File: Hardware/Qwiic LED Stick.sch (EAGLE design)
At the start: 39 parts, among them J2 SMD, J3 PTH, J4 SMD, J6 AVR_SPI_PROG_3X2TESTPOINTS, U1 Tiny85-20-SMT

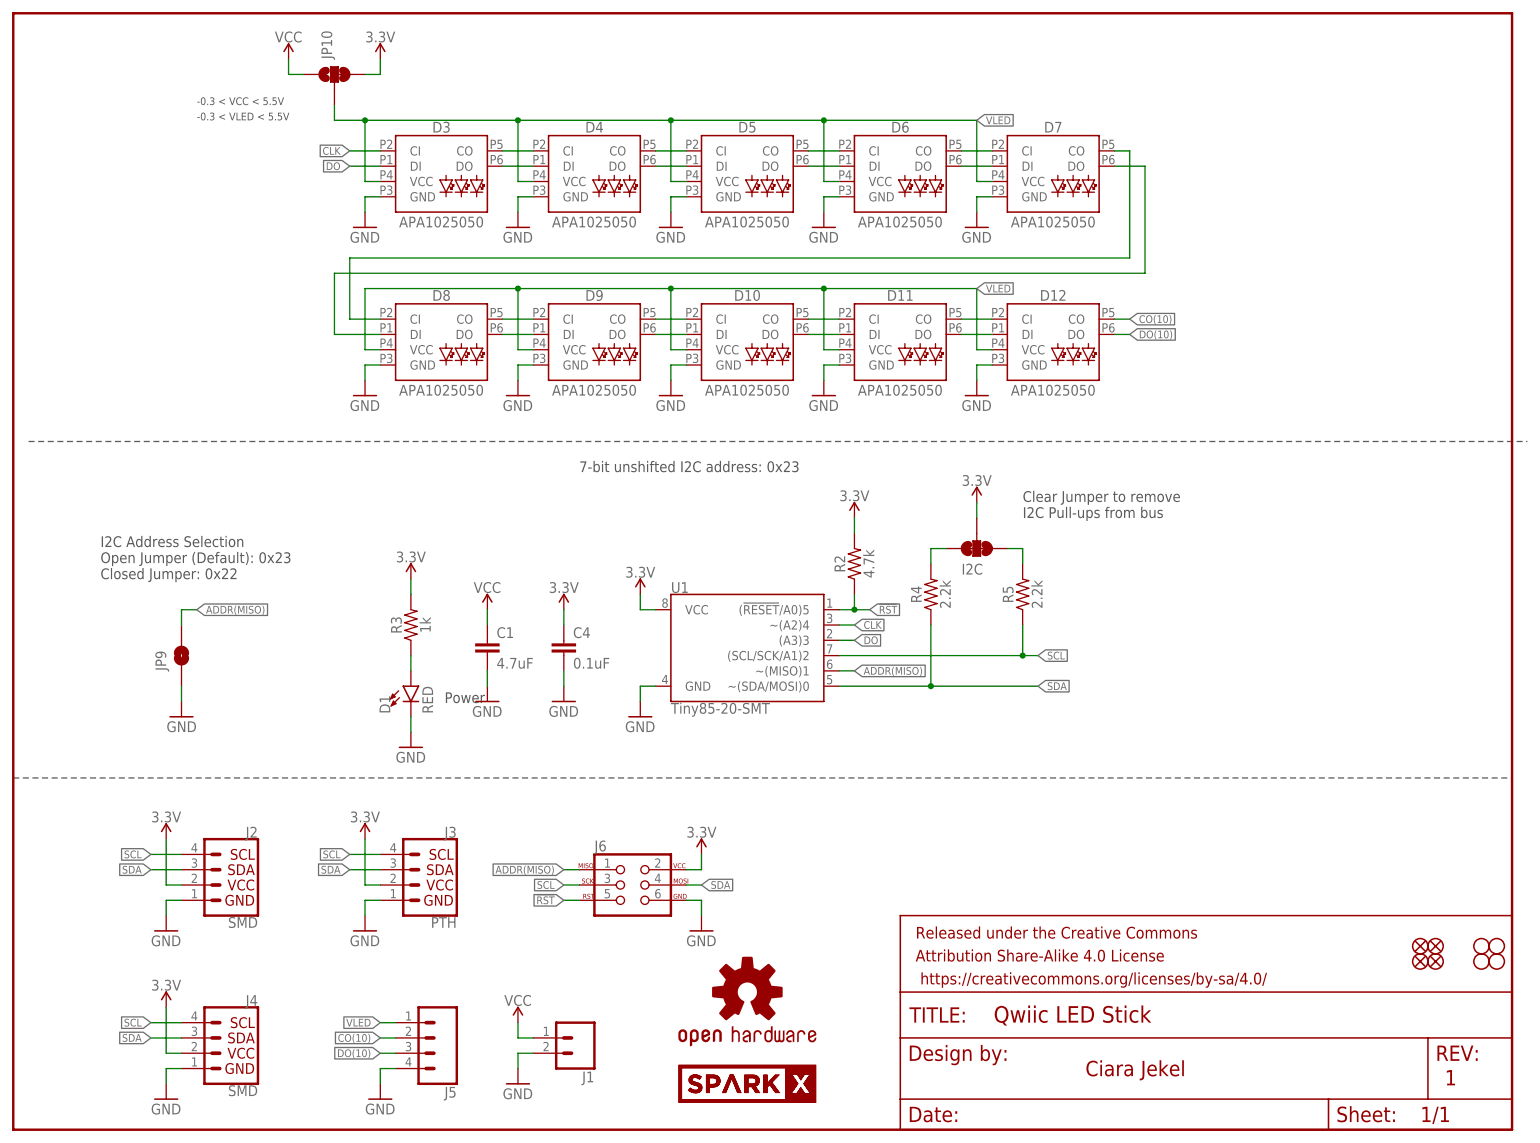
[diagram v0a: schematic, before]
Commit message: Update schematic and board for transition
Brought schematic and board routing up to current standards
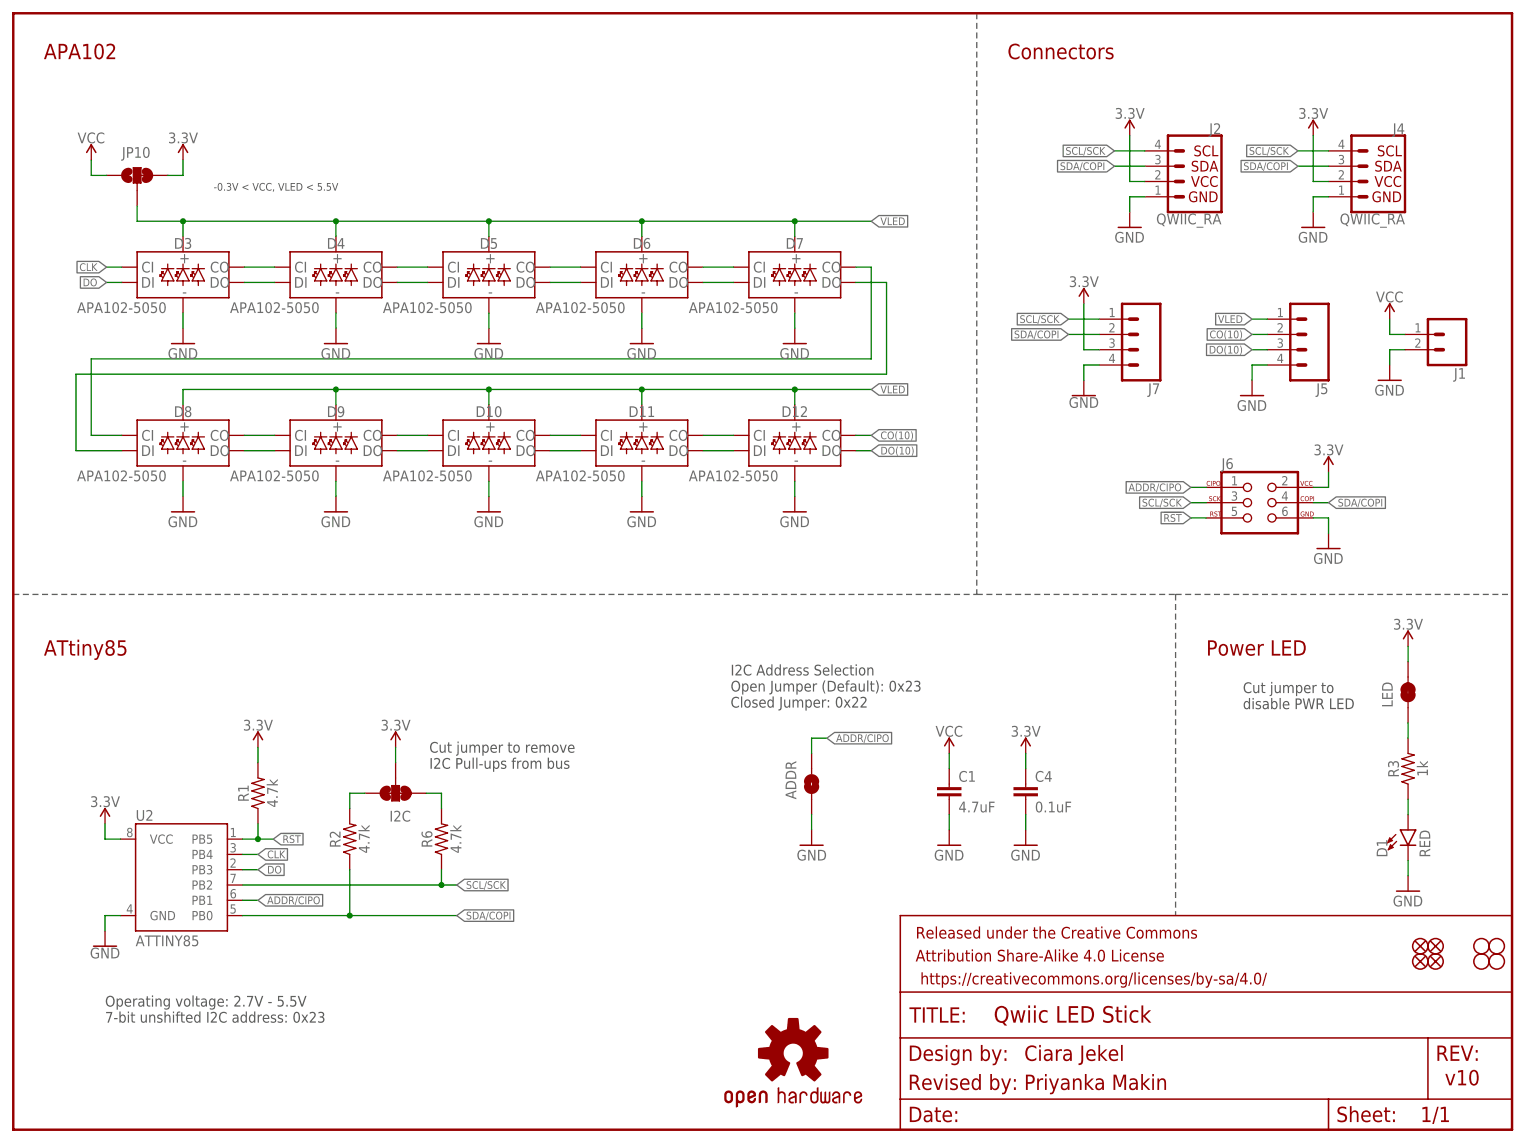
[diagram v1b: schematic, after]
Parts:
- removed J3: PTH, SparkX:I2C_STANDARD_NO_SILK
- removed JP9: JUMPER-SMT_2_NO_SILK, SparkFun-Jumpers:JUMPER-SMT_2_NO_SILK
- removed R4, R5: 2.2k, SparkFun-Resistors:2.2KOHM-0603-1/10W-1%
- removed U$1, U$2: SPARKX-LOGO4, SparkX:SPARKX-LOGO4
- removed U1: Tiny85-20-SMT, Qwiic-Bluetooth-HC1x:ATTINY85-ARDUINOTINY85-20-SMT
- added ADDR: JUMPER-SMT_2_NO_SILK, SparkFun-Jumpers:JUMPER-SMT_2_NO_SILK
- added J7: (no value), SparkFun-Connectors:CONN_041X04_NO_SILK_NO_POP
- added LED: JUMPER-SMT_2_NC_TRACE_SILK, SparkFun-Jumpers:JUMPER-SMT_2_NC_TRACE_SILK
- added R1, R6: 4.7k, SparkFun-Resistors:4.7KOHM-0603-1/10W-1%
- added U2: ATTINY85, SparkFun-IC-Microcontroller:ATTINY85
- D10, D11, D12, D3, D4, D5, D6, D7, D8, D9: value APA1025050 -> APA102-5050; device SparkFun-LED:APA1025050 -> SparkFun-LED:APA102-5050
- J2, J4: value SMD -> QWIIC_RA; device SparkX:I2C_STANDARDJS-1MM -> SparkFun-Connectors:QWIIC_CONNECTORJS-1MM
- JP1, JP2, JP5, JP6: device SparkFun:FIDUCIALUFIDUCIAL -> SparkFun-Aesthetics:FIDUCIALUFIDUCIAL
- JP3, JP4, JP7, JP8: device SparkFun:STAND-OFF -> SparkFun-Hardware:STAND-OFF
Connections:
- removed net ADDR(MISO): J6.1, JP9.2, U1.~(MISO)1
- removed net N$1: I2C.1, R5.2
- removed net N$2: I2C.3, R4.2
- removed net SCL: J2.SCL, J3.SCL, J4.SCL, J6.3, R5.1, U1.(SCL/SCK/A1)2
- removed net SDA: J2.SDA, J3.SDA, J4.SDA, J6.4, R4.1, U1.~(SDA/MOSI)0
- new net ADDR/CIPO: ADDR.2, J6.1, U2.PB1
- new net N$4: LED.1, R3.2
- new net N$5: I2C.3, R2.2
- new net N$6: I2C.1, R6.2
- new net SCL/SCK: J2.4, J4.4, J6.3, J7.1, R6.1, U2.PB2
- new net SDA/COPI: J2.3, J4.3, J6.4, J7.2, R2.1, U2.PB0
- net !RST: now also R1.1, U2.PB5; no longer R2.1, U1.(!RESET!/A0)5
- net 3.3V: now also J2.2, J4.2, J7.3, LED.2, R1.2, U2.VCC; no longer J2.VCC, J3.VCC, J4.VCC, R2.2, R3.2, U1.VCC
- net CLK: now also U2.PB4; no longer U1.~(A2)4
- net DO: now also U2.PB3; no longer U1.(A3)3
- net GND: now also ADDR.1, J2.1, J4.1, J7.4, U2.GND; no longer J2.GND, J3.GND, J4.GND, JP9.1, U1.GND
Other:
- note added: "-0.3V < VCC, VLED < 5.5V"
- note added: "APA102"
- note added: "ATtiny85"
- note added: "Connectors"
- note added: "Cut jumper to disable PWR LED"
- note added: "Cut jumper to remove I2C Pull-ups from bus"
- note added: "Operating voltage: 2.7V - 5.5V 7-bit unshifted I2C address: 0x23"
- note added: "Power LED"
- note added: "Revised by: Priyanka Makin"
- note added: "v10"
- note removed: "-0.3 < VCC < 5.5V"
- note removed: "-0.3 < VLED < 5.5V"
- note removed: "1"
- note removed: "7-bit unshifted I2C address: 0x23"
- note removed: "Clear Jumper to remove I2C Pull-ups from bus"
- note removed: "Power"
- moved on the sheet: C1, C4, D1, I2C, J1, J2, J4, J6, JP10, R2, R3
